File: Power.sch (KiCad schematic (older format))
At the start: 0 parts

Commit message: Added Power Protection And Filtering Schematic
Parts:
- added C? (x2): C, ~, symbol C
- added F? (x4): FUSE, ~, symbol FUSE
- added L? (x2): INDUCTOR, ~, symbol INDUCTOR
- added P?: CONN_12X2, symbol CONN_12X2
- added R?: R, ~, symbol R
- added SW?: SWITCH_INV, ~, symbol SWITCH_INV
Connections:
- new net: F?.1, P?.10 (P10)
- new net: F?.1, P?.14 (P14)
- new net: P?.16 (P16), SW?.2
- new net: F?.1, P?.2 (P2)
- new net: F?.1, P?.4 (P4), P?.6 (P6)
- new net: R?.1, SW?.1
- new net +12P: F?.2, L?.1
- new net +12V: C?.1, L?.2
- new net +3.3V: F?.2, R?.2
- new net +5V: F?.2
- new net -12P: F?.2, L?.1
- new net -12V: C?.2, L?.2
- new net GND: C?.1, C?.2, P?.3 (P3), P?.5 (P5), SW?.3

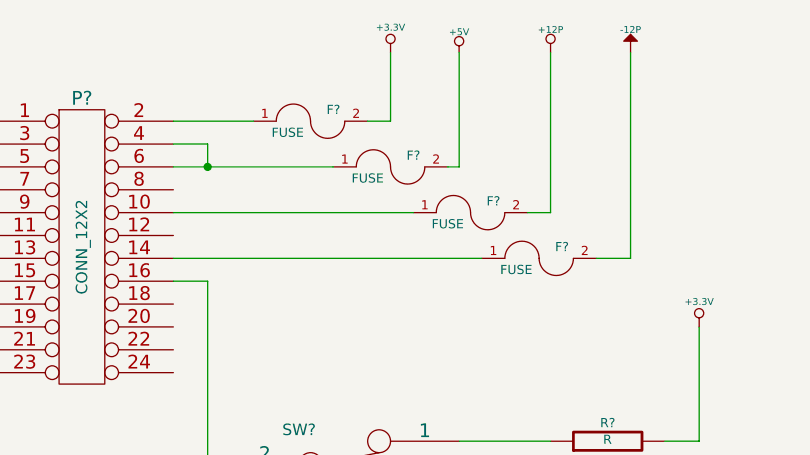
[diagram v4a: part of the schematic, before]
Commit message: Fan/Current Module Rework
Rework of the Fan/Current module
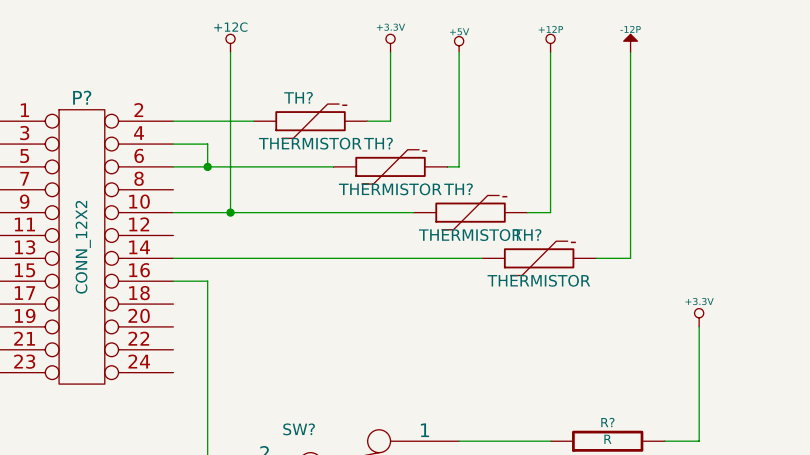
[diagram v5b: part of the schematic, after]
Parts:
- removed F? (x4): FUSE, ~, symbol FUSE
- added TH? (x4): THERMISTOR, ~, symbol THERMISTOR
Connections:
- net +12P: now also TH?.2
- net +3.3V: now also TH?.2
- net +5V: now also TH?.2
- net -12P: now also TH?.2
- net +12C: now reaches P?.10 (P10)
- net +12C: now also TH?.1
- net at P?.14 (P14): now also TH?.1
- net at P?.2 (P2): now also TH?.1
- net at P?.4 (P4), P?.6 (P6): now also TH?.1
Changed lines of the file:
@@
 $Descr A4 11693 8268
 encoding utf-8
-Sheet 5 9
+Sheet 4 9
 Title ""
 Date "28 sep 2013"
@@
 $EndComp
 $Comp
-L FUSE F?
-U 1 1 523FABBF
-P 3400 1500
-F 0 "F?" H 3500 1550 40  0000 C CNN
-F 1 "FUSE" H 3300 1450 40  0000 C CNN
-F 2 "~" H 3400 1500 60  0000 C CNN
-F 3 "~" H 3400 1500 60  0000 C CNN
-	1    3400 1500
-	1    0    0    -1
-$EndComp
-$Comp
-L FUSE F?
-U 1 1 523FABCC
-P 3750 1700
-F 0 "F?" H 3850 1750 40  0000 C CNN
-F 1 "FUSE" H 3650 1650 40  0000 C CNN
-F 2 "~" H 3750 1700 60  0000 C CNN
-F 3 "~" H 3750 1700 60  0000 C CNN
-	1    3750 1700
-	1    0    0    -1
-$EndComp
-$Comp
-L FUSE F?
-U 1 1 523FABD2
-P 4100 1900
-F 0 "F?" H 4200 1950 40  0000 C CNN
-F 1 "FUSE" H 4000 1850 40  0000 C CNN
-F 2 "~" H 4100 1900 60  0000 C CNN
-F 3 "~" H 4100 1900 60  0000 C CNN
-	1    4100 1900
-	1    0    0    -1
-$EndComp
-$Comp
-L FUSE F?
-U 1 1 523FABD8
-P 4400 2100
-F 0 "F?" H 4500 2150 40  0000 C CNN
-F 1 "FUSE" H 4300 2050 40  0000 C CNN
-F 2 "~" H 4400 2100 60  0000 C CNN
-F 3 "~" H 4400 2100 60  0000 C CNN
-	1    4400 2100
-	1    0    0    -1
-$EndComp
-$Comp
 L SWITCH_INV SW?
 U 1 1 523FAC1C
@@
 	9100 1550 9100 1400
 Connection ~ 8400 1550
+Wire Wire Line
+	3050 1900 3050 1200
+Connection ~ 3050 1900
+$Comp
+L +12C #PWR?
+U 1 1 52468F43
+P 3050 1200
+F 0 "#PWR?" H 3050 1170 30  0001 C CNN
+F 1 "+12C" H 3050 1310 40  0000 C CNN
+F 2 "" H 3050 1200 60  0000 C CNN
+F 3 "" H 3050 1200 60  0000 C CNN
+	1    3050 1200
+	1    0    0    -1
+$EndComp
+$Comp
+L THERMISTOR TH?
+U 1 1 52469215
+P 3400 1500
+F 0 "TH?" V 3500 1550 50  0000 C CNN
+F 1 "THERMISTOR" V 3300 1500 50  0000 C CNN
+F 2 "~" H 3400 1500 60  0000 C CNN
+F 3 "~" H 3400 1500 60  0000 C CNN
+	1    3400 1500
+	0    -1   -1   0
+$EndComp
+$Comp
+L THERMISTOR TH?
+U 1 1 52469222
+P 3750 1700
+F 0 "TH?" V 3850 1750 50  0000 C CNN
+F 1 "THERMISTOR" V 3650 1700 50  0000 C CNN
+F 2 "~" H 3750 1700 60  0000 C CNN
+F 3 "~" H 3750 1700 60  0000 C CNN
+	1    3750 1700
+	0    -1   -1   0
+$EndComp
+$Comp
+L THERMISTOR TH?
+U 1 1 52469228
+P 4100 1900
+F 0 "TH?" V 4200 1950 50  0000 C CNN
+F 1 "THERMISTOR" V 4000 1900 50  0000 C CNN
+F 2 "~" H 4100 1900 60  0000 C CNN
+F 3 "~" H 4100 1900 60  0000 C CNN
+	1    4100 1900
+	0    -1   -1   0
+$EndComp
+$Comp
+L THERMISTOR TH?
+U 1 1 5246922E
+P 4400 2100
+F 0 "TH?" V 4500 2150 50  0000 C CNN
+F 1 "THERMISTOR" V 4300 2100 50  0000 C CNN
+F 2 "~" H 4400 2100 60  0000 C CNN
+F 3 "~" H 4400 2100 60  0000 C CNN
+	1    4400 2100
+	0    -1   -1   0
+$EndComp
 $EndSCHEMATC

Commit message: Modified the Power Control module
Modified the Power Control module
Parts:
- added C?: C, ~, symbol C
- added L?: INDUCTOR, ~, symbol INDUCTOR
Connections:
- net +3.3V: no longer TH?.2
- net +5V: now also C?.1, L?.2; no longer TH?.2
- net GND: now also C?.2
- new net +3.3VP: TH?.2
- new net +5P: L?.1, TH?.2
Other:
- moved on the sheet: C?, L?
